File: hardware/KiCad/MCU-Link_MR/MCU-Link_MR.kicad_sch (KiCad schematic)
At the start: 8 parts

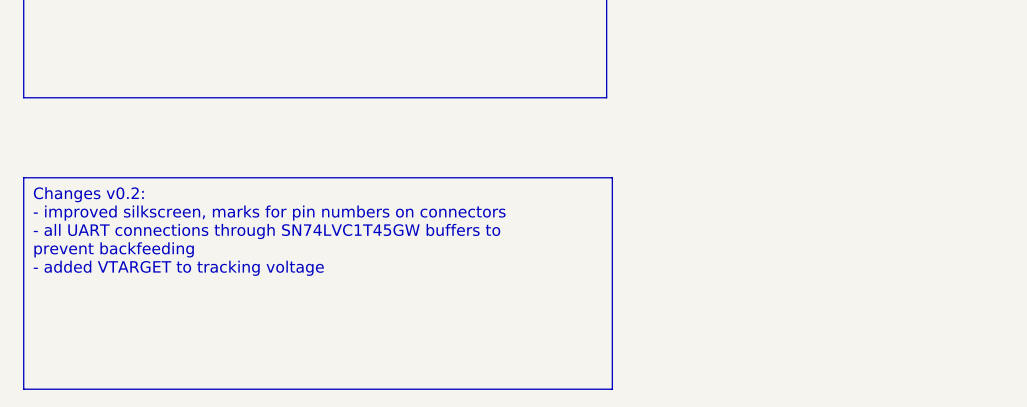
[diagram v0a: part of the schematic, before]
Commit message: sent v0.2 to PCB production
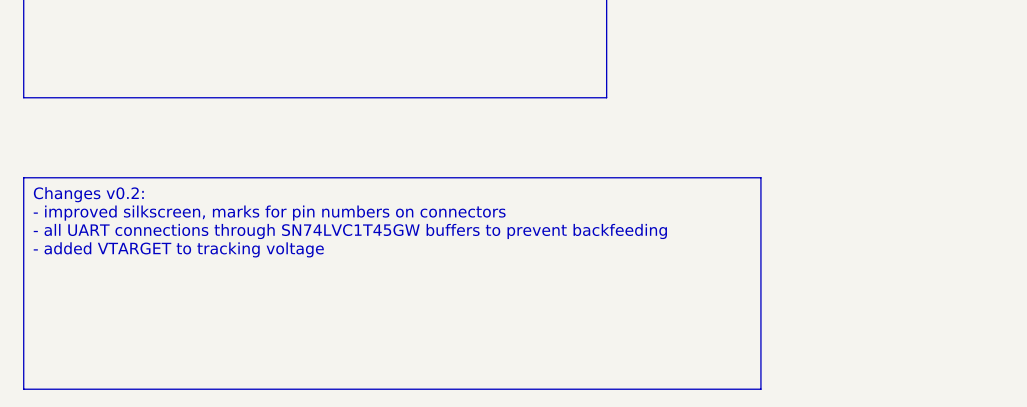
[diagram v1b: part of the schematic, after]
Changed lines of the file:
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@@
 		(exclude_from_sim no)
 		(at 26.035 105.41 0)
-		(size 65.405 23.495)
+		(size 81.915 23.495)
 		(stroke
 			(width 0)
